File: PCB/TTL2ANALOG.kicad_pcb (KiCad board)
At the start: 2 copper layers, 60.5 x 56.1 mm, 39 parts, among them J1 EGA/CGA, J2 Brown Fix, J3 CSync Inv., J4 Sync Type, J5 TTL Input, J6 Analog Out, J7 Barrel_Jack, U1 PAL20L8, U2 74LS244, U3 74LS244, U4 L78L05

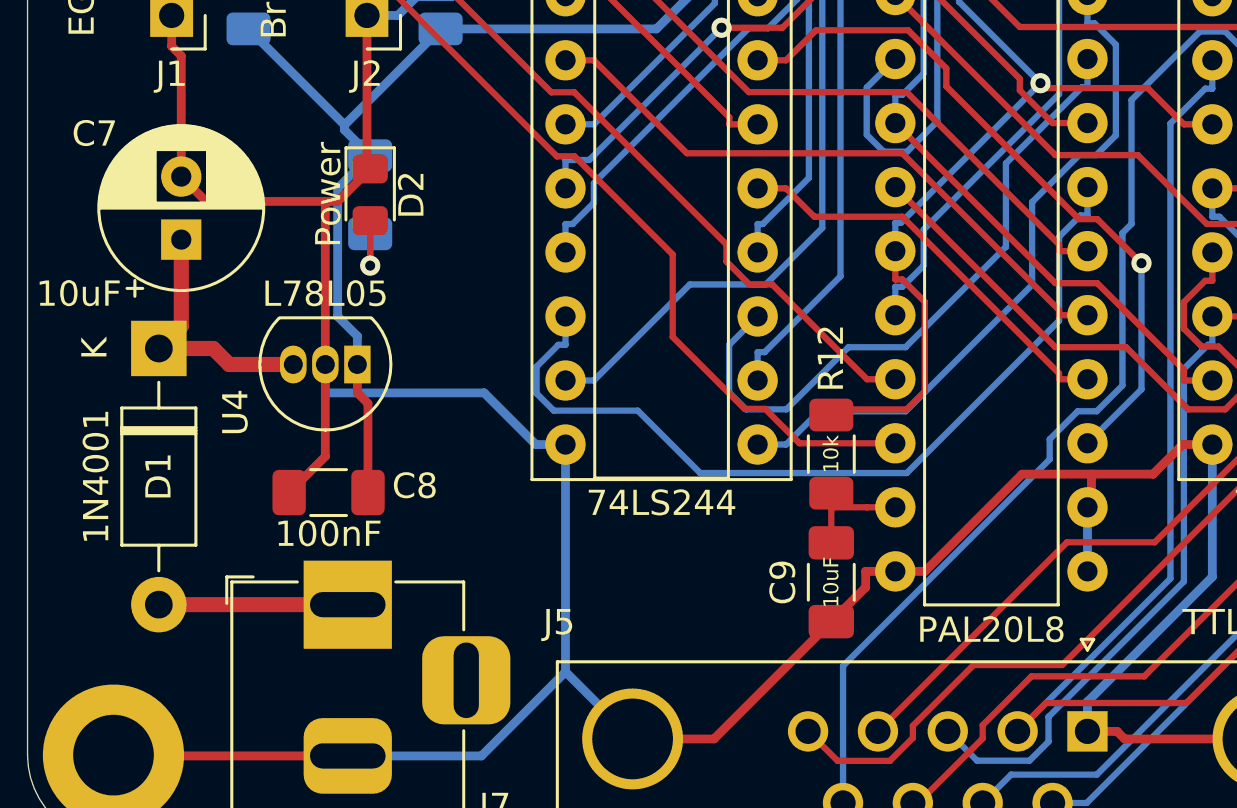
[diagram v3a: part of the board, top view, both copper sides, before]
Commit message: Use a TO220 7805 in new revision
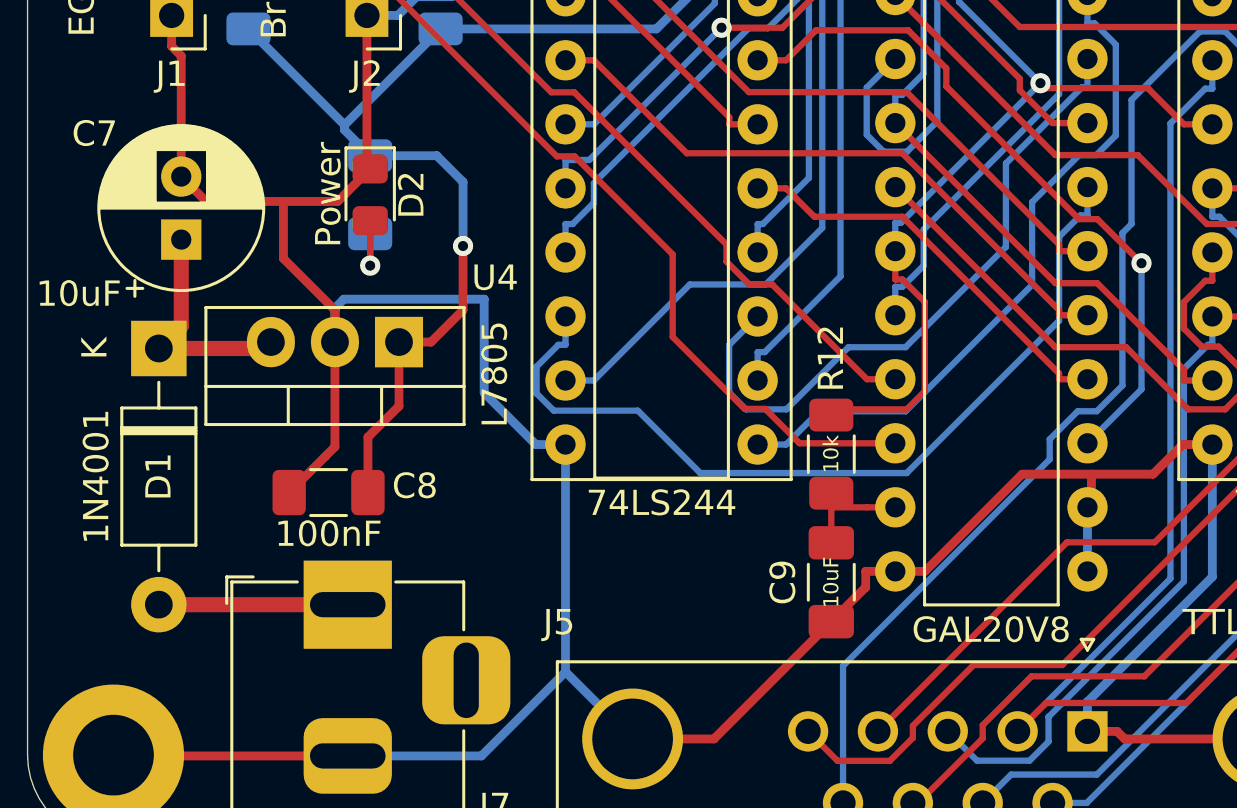
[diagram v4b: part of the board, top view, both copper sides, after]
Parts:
- R11: value 1k -> 1-4.7k
- R13: value 10k -> 0
- U1: value PAL20L8 -> GAL20V8
- U4: value L78L05 -> L7805; footprint Package_TO_SOT_THT:TO-92_Inline -> Package_TO_SOT_THT:TO-220-3_Vertical
- moved U4 1.88 mm to (121.9, 86.4)
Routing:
- net GND: track 276.5 -> 281.2 mm
- net VCC: track 109.1 -> 113.4 mm, vias 1 -> 2
- net Net-(C7-Pad1): track 10.3 -> 9.24 mm
